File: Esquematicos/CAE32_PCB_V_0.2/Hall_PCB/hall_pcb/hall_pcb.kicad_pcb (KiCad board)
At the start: 2 copper layers, 41 x 41 mm, 4 parts, among them J1 Conn_01x03_Female, U1 MT9105ET

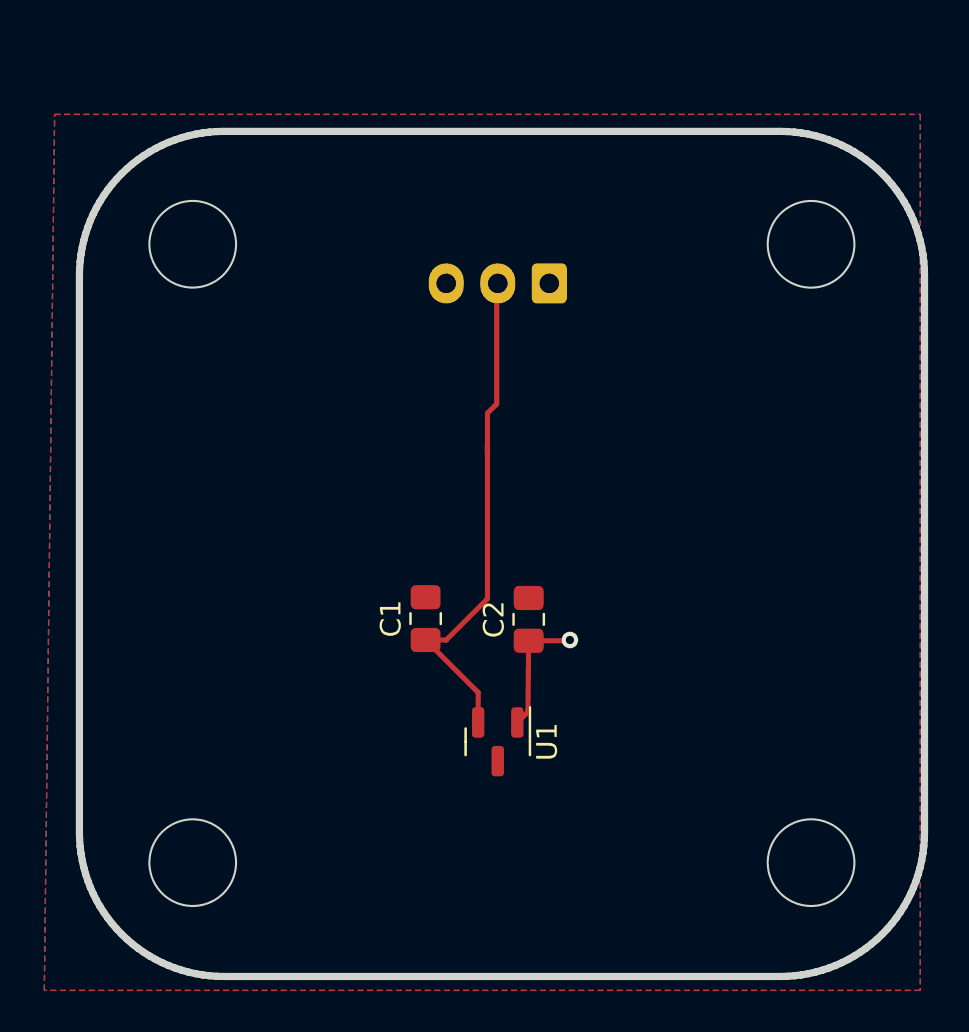
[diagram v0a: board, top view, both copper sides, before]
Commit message: Correciones de errores PCB:pedales y hall
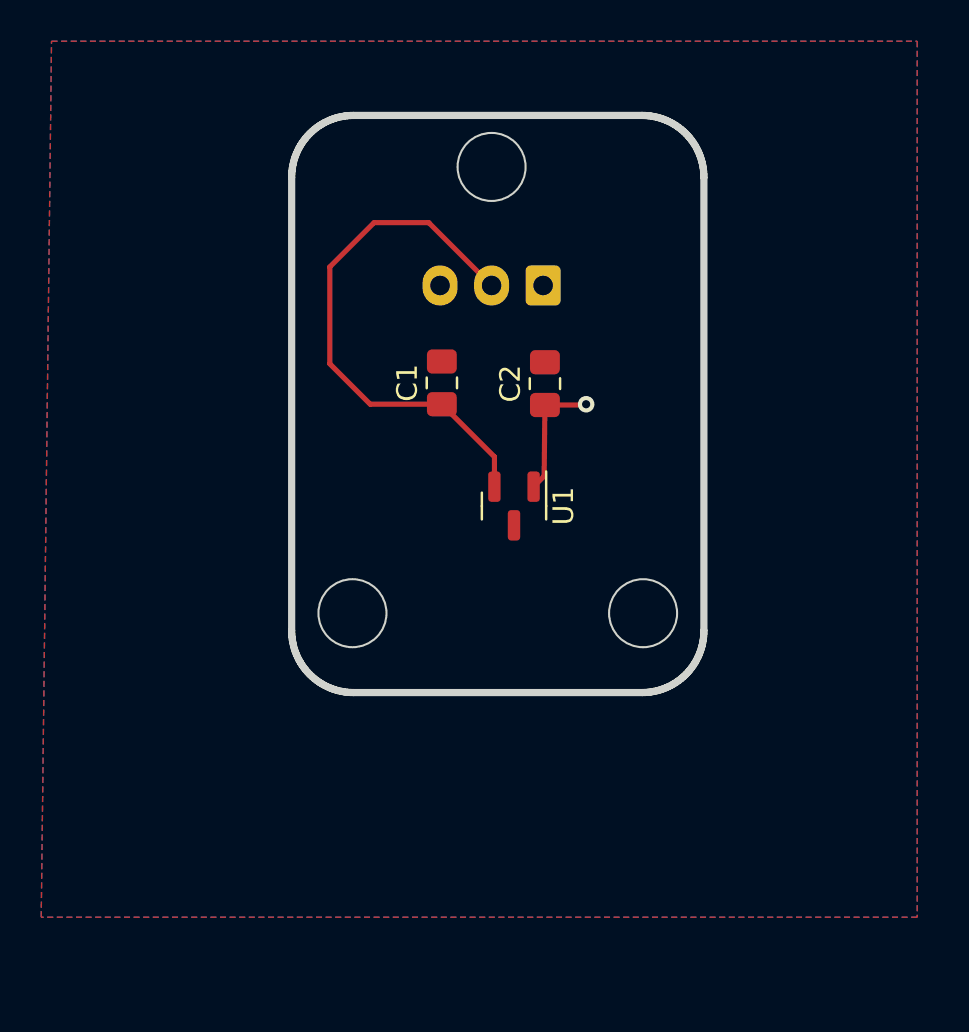
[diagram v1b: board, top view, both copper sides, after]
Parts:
- moved C1 11.5 mm to (132.8, 63.5)
- moved C2 11.5 mm to (137.8, 63.6)
- moved U1 11.5 mm to (136.3, 69.5)
- moved J1 0.32 mm to (137.7, 58.8)
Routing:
- net /Vout: track 24.8 -> 26.0 mm
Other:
- board size 41 x 41 mm -> 20 x 28 mm
